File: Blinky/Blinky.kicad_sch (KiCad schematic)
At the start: 76 parts, among them J1 Conn_01x06_Socket, J2 Conn_01x06_Socket, J3 Battery Connector, J4 Charging Notches, J5 Battery Connector, Q1 IRLML6244, Q2 IRLML6244, Q3 IRLML6244, Q4 IRLML6244, Q5 IRLML6244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

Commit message: new Board
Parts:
- U4: footprint footprint:SOIC-8_L4.9-W3.9-P1.27-LS6.0-BL -> footprint3:TSSOP-8_L4.4-W3.0-P0.65-LS6.4-BL-2
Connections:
- net PIN36: now also J1.5 (Pin_5); no longer J1.3 (Pin_3)
- net PIN37: now also J1.4 (Pin_4); no longer J1.2 (Pin_2)
- net PIN25: now reaches U3.25 (IO34)
- net PIN25: now also J1.2 (Pin_2)
- net PIN26: now reaches U3.26 (IO45)
- net PIN26: now also J1.3 (Pin_3)
- net PIN34: no longer names the net of U3.34 (IO41)
- net PIN34: no longer J1.4 (Pin_4)
- net PIN35: no longer names the net of U3.35 (IO42)
- net PIN35: no longer J1.5 (Pin_5)
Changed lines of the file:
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@@
 	(wire
 		(pts
+			(xy 212.09 149.86) (xy 220.98 149.86)
+		)
+		(stroke
+			(width 0)
+			(type default)
+		)
+	)
+	(wire
+		(pts
 			(xy 350.52 186.69) (xy 350.52 184.15)
 		)
@@
 	(wire
 		(pts
+			(xy 212.09 147.32) (xy 220.98 147.32)
+		)
+		(stroke
+			(width 0)
+			(type default)
+		)
+	)
+	(wire
+		(pts
 			(xy 179.07 124.46) (xy 189.23 124.46)
 		)
@@
 		)
 	)
-	(label "PIN34"
+	(label "PIN37"
 		(at 219.71 78.74 0)
 		(fields_autoplaced yes)
@@
 		)
 	)
-	(label "PIN35"
-		(at 214.63 124.46 0)
+	(label "PIN36"
+		(at 213.36 121.92 0)
 		(fields_autoplaced yes)
 		(effects
@@
 		)
 	)
-	(label "PIN36"
-		(at 213.36 121.92 0)
+	(label "PIN25"
+		(at 219.71 83.82 0)
 		(fields_autoplaced yes)
 		(effects
@@
 		)
 	)
-	(label "PIN37"
-		(at 219.71 83.82 0)
+	(label "PIN36"
+		(at 219.71 76.2 0)
 		(fields_autoplaced yes)
 		(effects
@@
 		)
 	)
-	(label "PIN35"
-		(at 219.71 76.2 0)
+	(label "PIN26"
+		(at 214.63 147.32 0)
 		(fields_autoplaced yes)
 		(effects
@@
 		)
 	)
-	(label "PIN34"
-		(at 213.36 127 0)
+	(label "PIN25"
+		(at 214.63 149.86 0)
 		(fields_autoplaced yes)
 		(effects
@@
 		)
 	)
-	(label "PIN36"
+	(label "PIN26"
 		(at 219.71 81.28 0)
 		(fields_autoplaced yes)
@@
 			)
 		)
-		(property "Footprint" "footprint:SOIC-8_L4.9-W3.9-P1.27-LS6.0-BL"
+		(property "Footprint" "footprint3:TSSOP-8_L4.4-W3.0-P0.65-LS6.4-BL-2"
 			(at 311.15 191.77 0)
 			(effects
@@
 			)
 		)
-		(property "Footprint" "footprint:SOIC-8_L4.9-W3.9-P1.27-LS6.0-BL"
+		(property "Footprint" "footprint3:TSSOP-8_L4.4-W3.0-P0.65-LS6.4-BL-2"
 			(at 276.86 191.77 0)
 			(effects

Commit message: updated pcb
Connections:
- net GND: now also U6.9 (EP)
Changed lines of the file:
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@@
+	(symbol
+		(lib_id "power:GND")
+		(at 346.71 91.44 90)
+		(unit 1)
+		(exclude_from_sim no)
+		(in_bom yes)
+		(on_board yes)
+		(dnp no)
+		(property "Reference" "#PWR048"
+			(at 353.06 91.44 0)
+			(effects
+				(font
+					(size 1.27 1.27)
+				)
+				(hide yes)
+			)
+		)
+		(property "Value" "GND"
+			(at 350.52 91.44 90)
+			(effects
+				(font
+					(size 1.27 1.27)
+				)
+				(justify right)
+			)
+		)
+		(property "Footprint" ""
+			(at 346.71 91.44 0)
+			(effects
+				(font
+					(size 1.27 1.27)
+				)
+				(hide yes)
+			)
+		)
+		(property "Datasheet" ""
+			(at 346.71 91.44 0)
+			(effects
+				(font
+					(size 1.27 1.27)
+				)
+				(hide yes)
+			)
+		)
+		(property "Description" ""
+			(at 346.71 91.44 0)
+			(effects
+				(font
+					(size 1.27 1.27)
+				)
+				(hide yes)
+			)
+		)
+		(pin "1"
+		)
+		(instances
+			(project "Blinky"
+				(path "/a854b35b-60aa-44a5-a34e-fbb2d526cb93"
+					(reference "#PWR048")
+					(unit 1)
+				)
+			)
+		)
+	)
 	(symbol
 		(lib_id "power:GND")

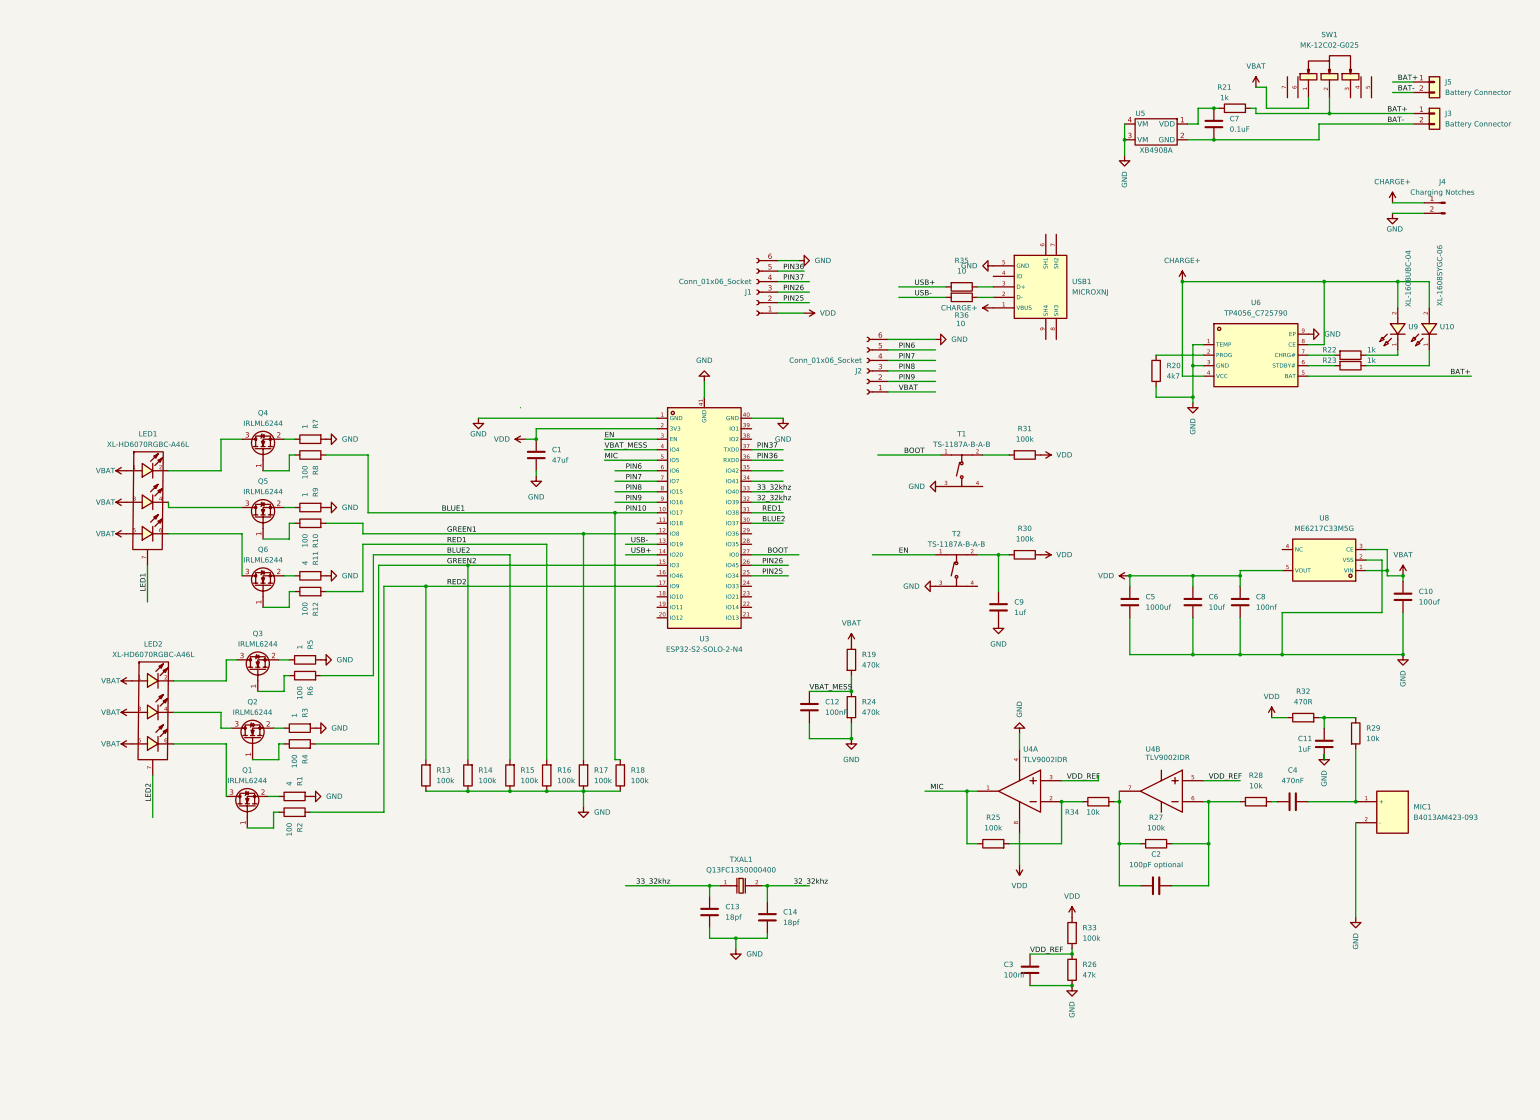
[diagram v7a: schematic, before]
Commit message: C1 größerer Footprint Layout angepasst, geprüft Fehlende Footprints ergänzt.
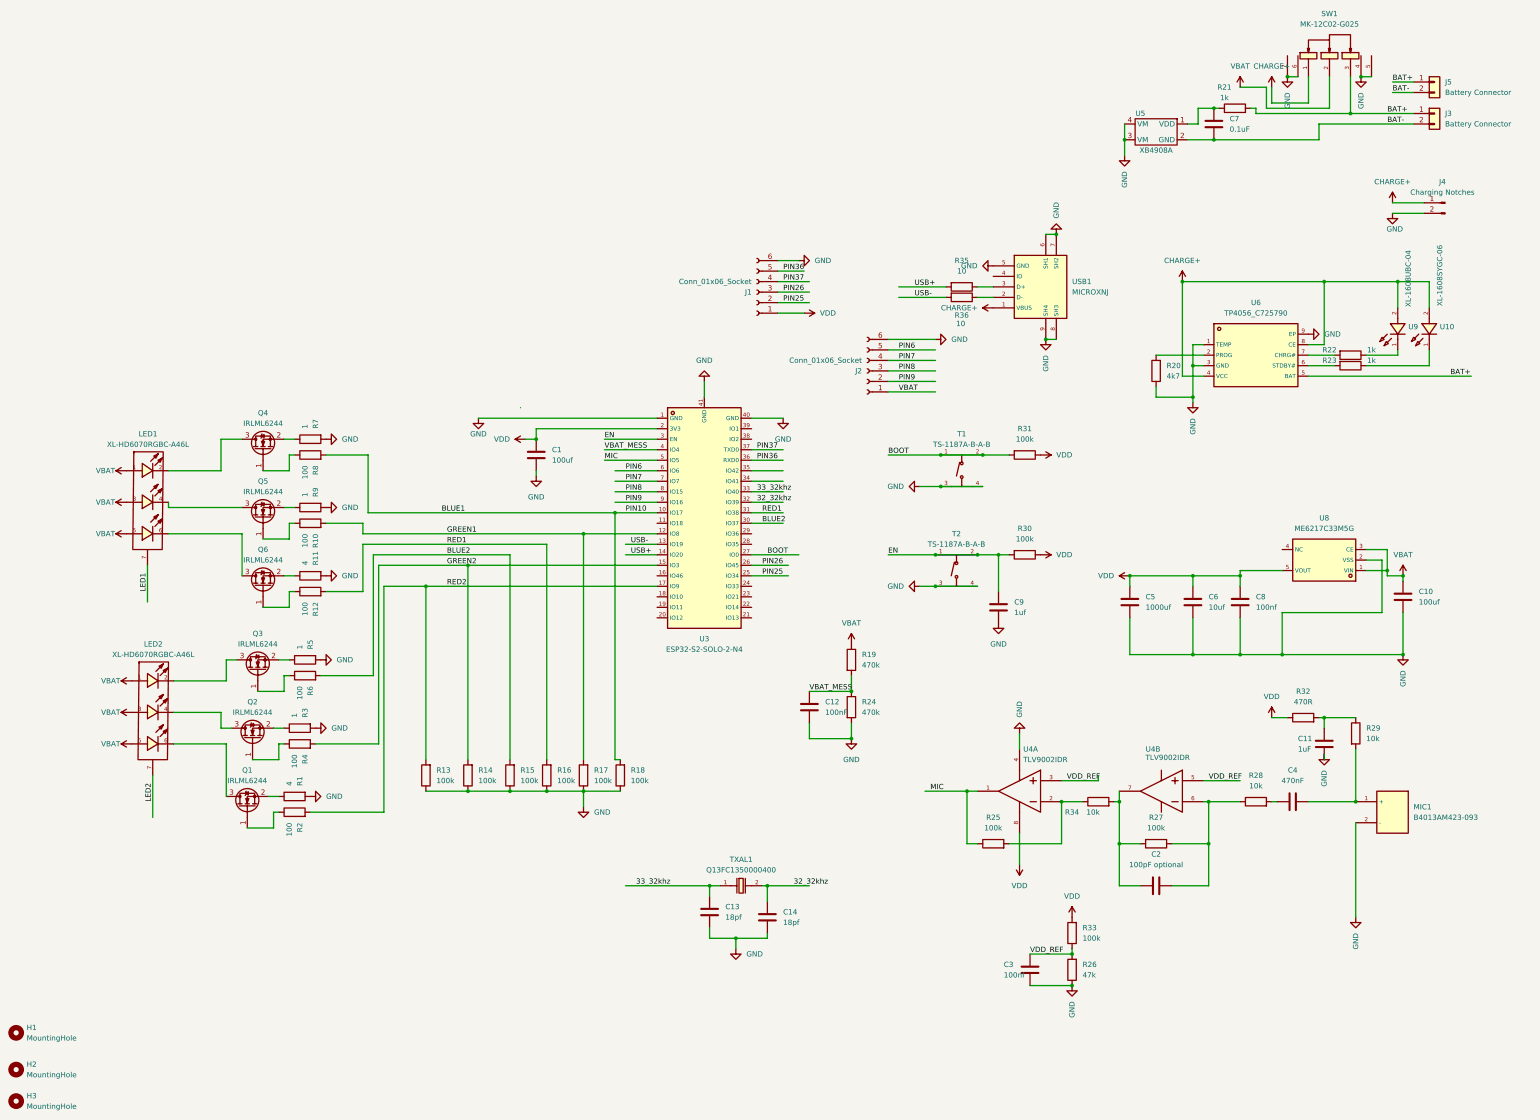
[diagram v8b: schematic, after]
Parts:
- added H1, H2, H3: MountingHole, MountingHole:MountingHole_3.2mm_M3, symbol Mechanical:MountingHole
- C1: value 47uf -> 100uf; footprint Capacitor_SMD:C_0603_1608Metric -> Library:CASE-B_3528
- C10: footprint footprint:CASE-B_3528 -> Library:CASE-B_3528
- C5: footprint footprint6:CAP-SMD_BD8.0-L8.3-W8.3-FD -> Library:CAP-SMD_BD8.0-L8.3-W8.3-FD
- J1, J2: footprint footprint:HDR-TH_6P-P2.54-V-F -> Library:HDR-TH_6P-P2.54-V-F
- MIC1: footprint footprint:MIC-TH_BD6.0_B6027AP383-056 -> Library:MIC-TH_BD6.0_B6027AP383-056
- SW1: footprint footprint:SW-SMD_MK-12C02-G025 -> Library:SW-SMD_MK-12C02-G025
- T1, T2: footprint footprint:SW-SMD_4P-L5.1-W5.1-P3.70-LS6.5-TL-2 -> Library:SW-SMD_4P-L5.1-W5.1-P3.70-LS6.5-TL-2
- TXAL1: footprint footprint3:FC-135R_L3.2-W1.5 -> Crystal:Crystal_SMD_3215-2Pin_3.2x1.5mm
- U10: footprint footprint:LED0603-RD_GREEN -> Library:LED0603-RD_GREEN
- U3: footprint footprint:WIRELM-SMD_ESP32-S3-WROOM-1 -> Library:WIRELM-SMD_ESP32-S3-WROOM-1
- U4: footprint footprint3:TSSOP-8_L4.4-W3.0-P0.65-LS6.4-BL-2 -> Library:TSSOP-8_L4.4-W3.0-P0.65-LS6.4-BL-2
- U5: footprint footprint:XB4908A -> Library:XB4908A
- U6: footprint footprint:ESOP-8_L4.9-W3.9-P1.27-LS6.0-BL-EP -> Library:ESOP-8_L4.9-W3.9-P1.27-LS6.0-BL-EP
- U8: footprint footprint:SOT-23-5_L3.0-W1.7-P0.95-LS2.8-BR -> Library:SOT-23-5_L3.0-W1.7-P0.95-LS2.8-BR
- U9: footprint footprint:LED0603-RD_BLUE -> Library:LED0603-RD_BLUE
- USB1: footprint footprint:MICRO-USB-SMD_MICROXNJ -> Library:MICRO-USB-SMD_MICROXNJ
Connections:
- net BAT+: now also SW1.3; no longer SW1.2
- net BOOT: now also R31.2, T1.2 (B)
- net CHARGE+: now also SW1.1
- net EN: now also C9.2, R30.2, T2.2 (B)
- net GND: now also C1.2, SW1.4, SW1.5, SW1.6, SW1.7, T1.4 (D), T2.4 (D), USB1.6 (SH1), USB1.7 (SH2), USB1.8 (SH3), USB1.9 (SH4); no longer C1.1
- net VBAT: now also SW1.2; no longer SW1.1
- net VDD: now also C1.1; no longer C1.2
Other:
- moved on the sheet: SW1
